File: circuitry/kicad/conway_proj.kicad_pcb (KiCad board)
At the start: 2 copper layers, 68.6 x 53.3 mm, 9 parts, among them J1 Power, J2 Digital/PWM, J3 Analog, J4 Digital/PWM

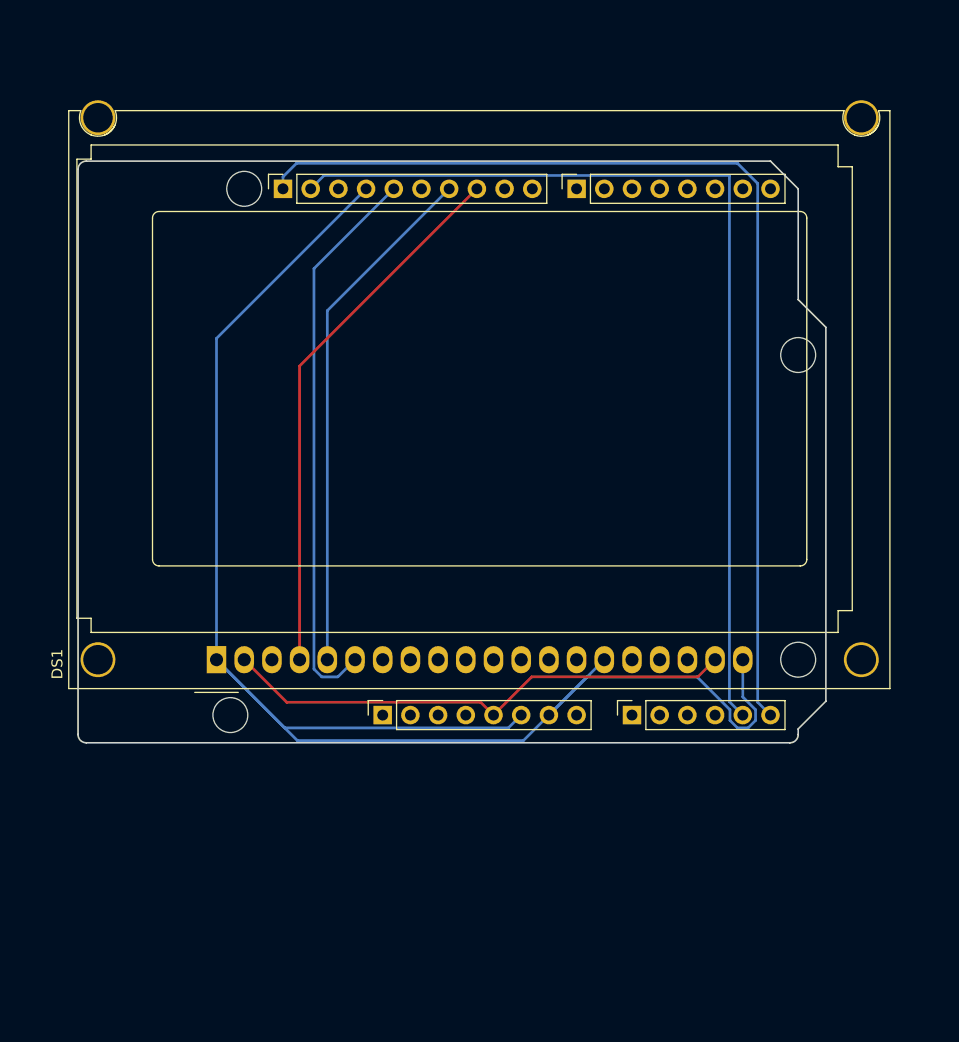
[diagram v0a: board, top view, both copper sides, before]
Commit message: New KiCad version and README updates
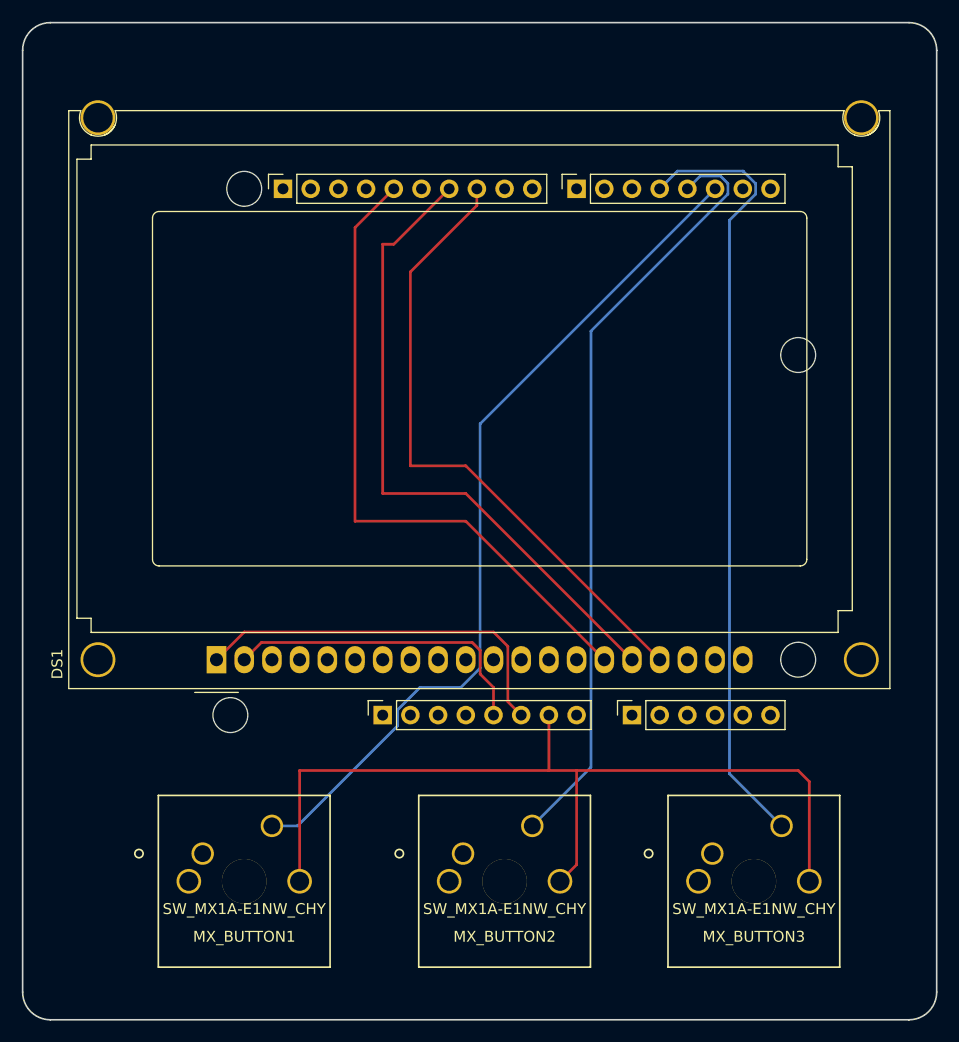
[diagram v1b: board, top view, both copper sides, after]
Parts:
- added G***: LOGO, LOGO, B.Cu at (102.5, 138.1)
- added MX_BUTTON1: SW_MX1A-E1NW_CHY, MX1A-E1NW:MX1A-E1NW, F.Cu at (86.0, 176.2)
- added MX_BUTTON2: SW_MX1A-E1NW_CHY, MX1A-E1NW:MX1A-E1NW, F.Cu at (109.9, 176.2)
- added MX_BUTTON3: SW_MX1A-E1NW_CHY, MX1A-E1NW:MX1A-E1NW, F.Cu at (132.8, 176.2)
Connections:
- net /*9 renamed 9
- net /8 renamed 8
- DS1 pad 10: unconnected-(DS1-DB3-Pad10) -> /passive
- DS1 pad 11: unconnected-(DS1-DB4-Pad11) -> /passive
- DS1 pad 12: unconnected-(DS1-DB5-Pad12) -> /passive
- DS1 pad 13: unconnected-(DS1-DB6-Pad13) -> /passive
- DS1 pad 14: unconnected-(DS1-DB7-Pad14) -> /passive
- DS1 pad 15: GND -> /13
- DS1 pad 16: unconnected-(DS1-NC-Pad16) -> /*11
- DS1 pad 17: unconnected-(DS1-RST-Pad17) -> /*10
- DS1 pad 18: unconnected-(DS1-VOUT-Pad18) -> /passive
- DS1 pad 3: unconnected-(DS1-VO-Pad3) -> /passive
- DS1 pad 4: /*10 -> /passive
- DS1 pad 5: /*11 -> /passive
- DS1 pad 6: /13 -> GND
- DS1 pad 7: unconnected-(DS1-DB0-Pad7) -> /passive
- DS1 pad 8: unconnected-(DS1-DB1-Pad8) -> /passive
- DS1 pad 9: unconnected-(DS1-DB2-Pad9) -> /passive
- J3 pad 4: /A3 -> GND
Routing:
- net /SCL/A5: track 95.1 -> 0.00 mm
- net /SDA/A4: track 88.9 -> 0.00 mm
- net /2: track 0.00 -> 78.8 mm
- net /4: track 0.00 -> 71.8 mm
- net /*3: track 0.00 -> 70.8 mm
- net GND: track 150.8 -> 117.5 mm
- net +5V: track 47.4 -> 29.0 mm
- net /*11: track 47.8 -> 60.2 mm
- net /13: track 51.8 -> 60.1 mm
- net /*10: track 49.9 -> 58.1 mm
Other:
- board size 68.6 x 53.3 mm -> 83.8 x 91.4 mm
- board text added: "LCD + buttons Arduino Uno Breakout board Designed by Shaun Lowis"

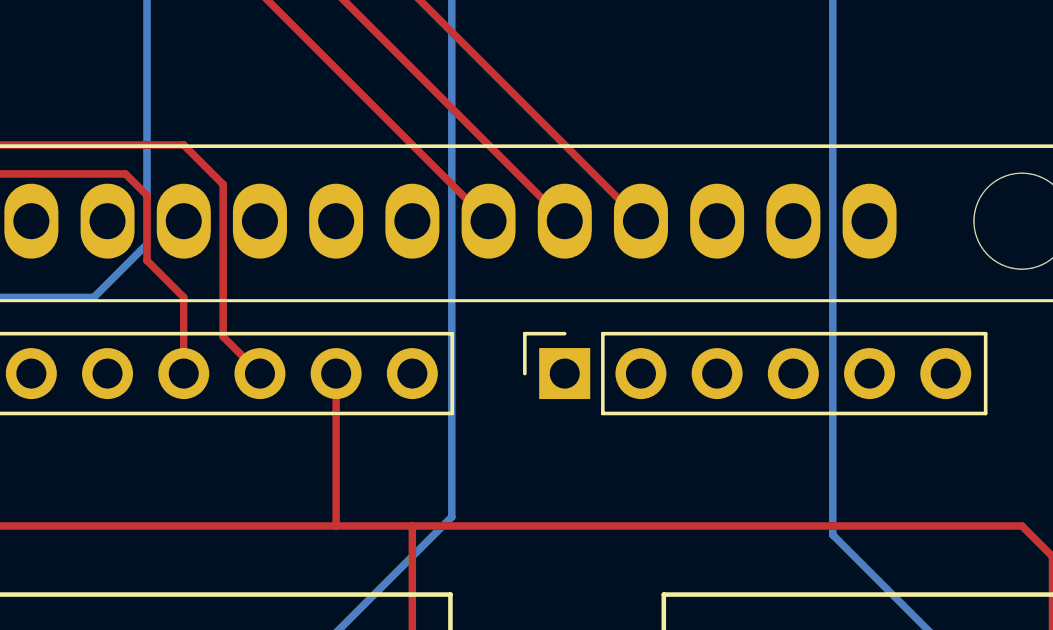
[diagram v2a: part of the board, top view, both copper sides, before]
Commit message: Updated PCB layout, fixed 5V and ground to LCD connections.
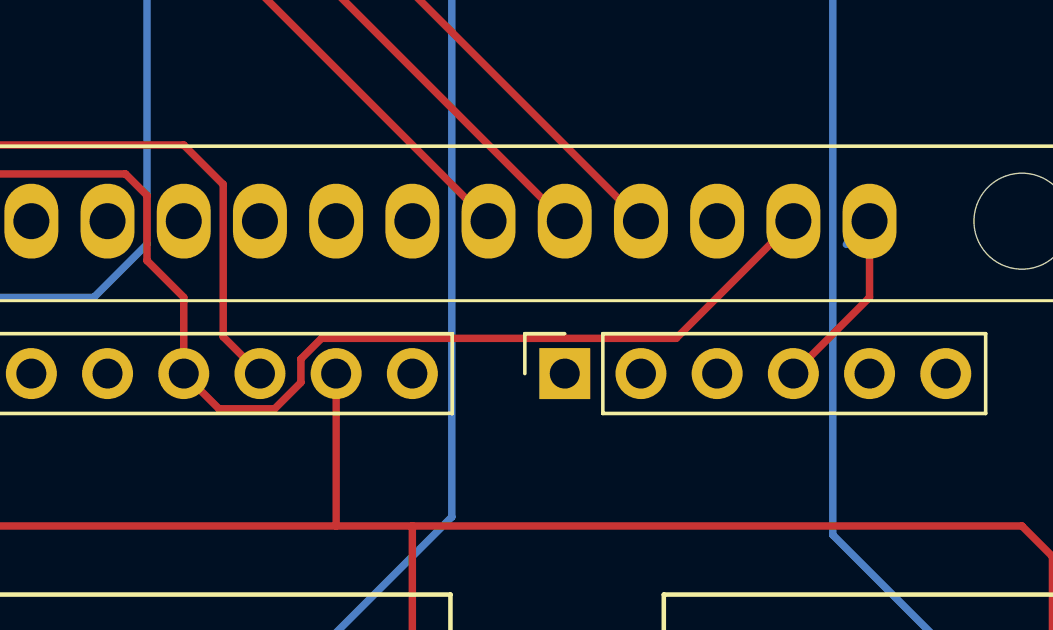
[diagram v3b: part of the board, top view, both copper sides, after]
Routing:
- net +5V: track 29.0 -> 52.9 mm
- net GND: track 117.5 -> 124.7 mm
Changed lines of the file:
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@@
   )
   (segment (start 112.7 155.88) (end 114.015 157.195) (width 0.25) (layer "F.Cu") (net 1))
+  (segment (start 135.56 158.42) (end 135.56 160.96) (width 0.25) (layer "F.Cu") (net 1))
   (segment (start 117.78 163.5) (end 117.78 168.58) (width 0.25) (layer "F.Cu") (net 1))
   (segment (start 114.015 157.195) (end 114.015 162.275) (width 0.25) (layer "F.Cu") (net 1))
@@
   (segment (start 89.84 155.88) (end 112.7 155.88) (width 0.25) (layer "F.Cu") (net 1))
   (segment (start 140.64 168.58) (end 141.656 169.596) (width 0.25) (layer "F.Cu") (net 1))
+  (segment (start 135.56 160.96) (end 133.02 163.5) (width 0.25) (layer "F.Cu") (net 1))
   (segment (start 120.32 177.216) (end 120.32 168.58) (width 0.25) (layer "F.Cu") (net 1))
   (segment (start 87.3 158.42) (end 89.84 155.88) (width 0.25) (layer "F.Cu") (net 1))
   (segment (start 117.78 168.58) (end 120.32 168.58) (width 0.25) (layer "F.Cu") (net 1))
+  (segment (start 135.56 158.42) (end 134.785 159.195) (width 0.25) (layer "B.Cu") (net 1))
   (segment (start 112.7 160.96) (end 112.7 163.5) (width 0.25) (layer "F.Cu") (net 3))
   (segment (start 89.84 158.42) (end 91.415 156.845) (width 0.25) (layer "F.Cu") (net 3))
+  (segment (start 116.605 163.796701) (end 115.726701 164.675) (width 0.25) (layer "F.Cu") (net 3))
   (segment (start 111.475 157.562588) (end 111.475 159.735) (width 0.25) (layer "F.Cu") (net 3))
   (segment (start 111.475 159.735) (end 112.7 160.96) (width 0.25) (layer "F.Cu") (net 3))
+  (segment (start 117.293299 162.325) (end 116.605 163.013299) (width 0.25) (layer "F.Cu") (net 3))
+  (segment (start 113.875 164.675) (end 112.7 163.5) (width 0.25) (layer "F.Cu") (net 3))
+  (segment (start 129.115 162.325) (end 117.293299 162.325) (width 0.25) (layer "F.Cu") (net 3))
+  (segment (start 133.02 158.42) (end 129.115 162.325) (width 0.25) (layer "F.Cu") (net 3))
+  (segment (start 115.726701 164.675) (end 113.875 164.675) (width 0.25) (layer "F.Cu") (net 3))
   (segment (start 91.415 156.845) (end 110.757412 156.845) (width 0.25) (layer "F.Cu") (net 3))
   (segment (start 110.757412 156.845) (end 111.475 157.562588) (width 0.25) (layer "F.Cu") (net 3))
+  (segment (start 116.605 163.013299) (end 116.605 163.796701) (width 0.25) (layer "F.Cu") (net 3))
   (segment (start 110.16 145.72) (end 100 145.72) (width 0.25) (layer "F.Cu") (net 10))
   (segment (start 100 118.796) (end 103.556 115.24) (width 0.25) (layer "F.Cu") (net 10))
